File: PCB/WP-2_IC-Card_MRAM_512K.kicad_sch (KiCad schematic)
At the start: 25 parts, among them J1 SMS-138-01-G-S, SW1 CUS-14TB, U1 MR2A08xxYSxxx, U2 MIC5317-3.3YD5, U3 4245, U4 4245, U5 4245, U6 4245

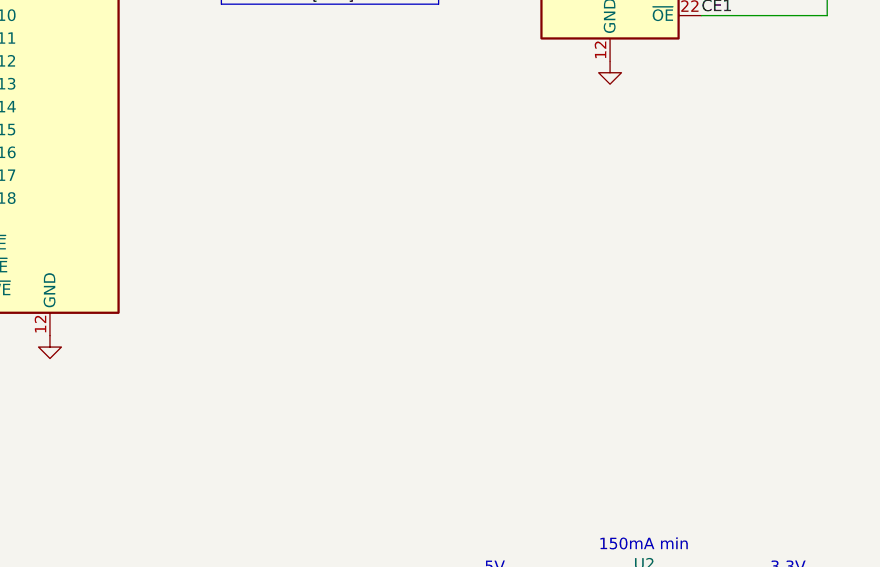
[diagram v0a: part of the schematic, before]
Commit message: mram specify industrial part
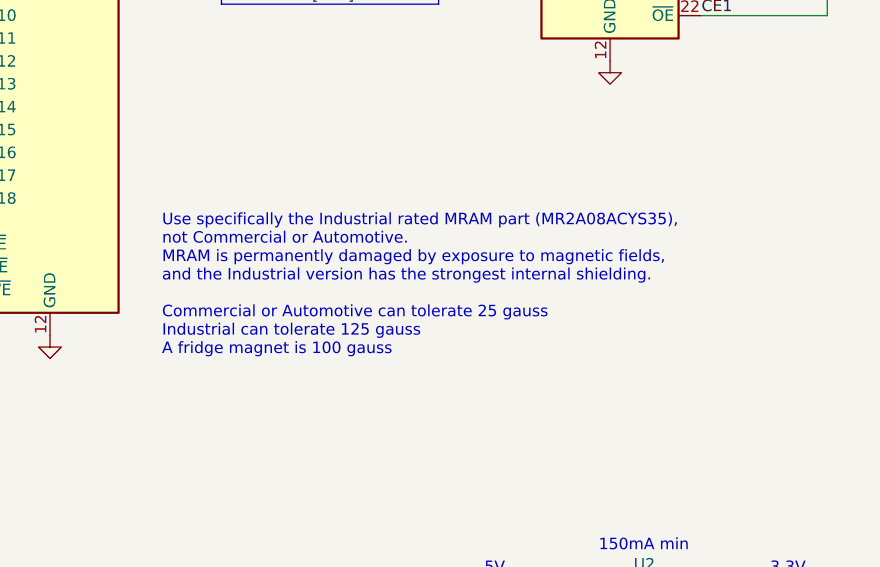
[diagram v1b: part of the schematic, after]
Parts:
- U1: MPN MR2A08AYS35 -> MR2A08ACYS35
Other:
- note added: "Use specifically the Industrial rated MRAM part (MR2A08ACYS35), not Commercial or Automotive. MRAM is permanently damaged by exposure to magnetic fields, and the Industrial version has the strongest internal shielding. Commercial or Automotive can tolerate 25 gauss Industrial can tolerate 125 gauss A fridge magnet is 100 gauss"
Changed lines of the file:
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@@
 		)
 	)
+	(text "Use specifically the Industrial rated MRAM part (MR2A08ACYS35),\nnot Commercial or Automotive.\nMRAM is permanently damaged by exposure to magnetic fields,\nand the Industrial version has the strongest internal shielding.\n\nCommercial or Automotive can tolerate 25 gauss\nIndustrial can tolerate 125 gauss\nA fridge magnet is 100 gauss\n"
+		(exclude_from_sim no)
+		(at 177.546 102.108 0)
+		(effects
+			(font
+				(size 1.27 1.27)
+			)
+			(justify left top)
+		)
+	)
 	(text "5V"
 		(exclude_from_sim no)
@@
 			)
 		)
-		(property "MPN" "MR2A08AYS35"
+		(property "MPN" "MR2A08ACYS35"
 			(at 165.1 82.55 0)
 			(effects

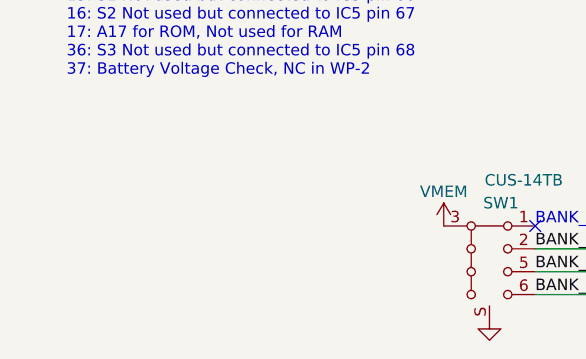
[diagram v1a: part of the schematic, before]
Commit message: local symbol & footprint library organization, add shielded mram version
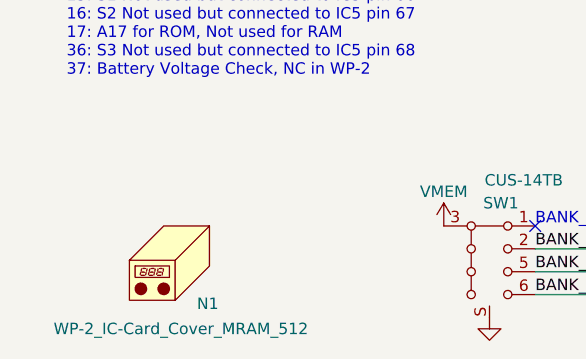
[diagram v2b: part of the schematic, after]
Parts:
- added N1: WP-2_IC-Card_Cover_MRAM_512, 000_LOCAL:WP-2_IC_Card_Cover_MRAM_512, symbol 000_LOCAL:Housing
- C1, C10, C11, C12, C2, C3, C4, C5, C6, C7, C8, C9: footprint 0_LOCAL:C_0805_1mm -> 000_LOCAL:C_0805_1mm; symbol 0_LOCAL:C_Small -> 000_LOCAL:C_Small
- D1: footprint 0_LOCAL:TSSOP-6-symmetric -> 000_LOCAL:TSSOP-6-symmetric; symbol 0_LOCAL:BAT54CDW -> 000_LOCAL:BAT54CDW
- J1: footprint 0_LOCAL:SMS-138-01-x-x_edge -> 000_LOCAL:SMS-138-01-x-x_pcb_edge; symbol 0_LOCAL:Conn_01x38_Female -> 000_LOCAL:Conn_01x38_Female
- R1, R2, R3, R4: footprint 0_LOCAL:R_0805 -> 000_LOCAL:R_0805; symbol 0_LOCAL:R -> 000_LOCAL:R
- SW1: footprint 0_LOCAL:SW_SP4T_CUS-14B pth -> 000_LOCAL:SW_SP4T_CUS-14B pth; symbol 0_LOCAL:SW_1P4T_CUS-14B -> 000_LOCAL:SW_1P4T_CUS-14B
- U1: footprint 0_LOCAL:TSOP-II-44_10.16x18.41mm_P0.8mm -> 000_LOCAL:TSOP-II-44_10.16x18.41mm_P0.8mm; symbol 0_LOCAL:MR2A08xxYSxxx -> 000_LOCAL:MR2A08xxYSxxx
- U2: footprint 0_LOCAL:TSOT-23-5 -> 000_LOCAL:TSOT-23-5; symbol 0_LOCAL:MIC5365-3.3YD5 -> 000_LOCAL:MIC5365-3.3YD5
- U3, U4, U5, U6: footprint 0_LOCAL:TSSOP-24_4.4x7.8mm_P0.65mm -> 000_LOCAL:TSSOP-24_4.4x7.8mm_P0.65mm; symbol 0_LOCAL:4245 -> 000_LOCAL:4245

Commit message: cleanup names, cover inside corner reliefs
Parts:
- N1: footprint 000_LOCAL:WP-2_IC_Card_Cover_MRAM_512 -> 000_LOCAL:WP-2_IC-Card_Cover_MRAM_512; now left out of the parts list
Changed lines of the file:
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@@
 		(unit 1)
 		(exclude_from_sim yes)
-		(in_bom yes)
+		(in_bom no)
 		(on_board yes)
 		(dnp no)
@@
 			)
 		)
-		(property "Footprint" "000_LOCAL:WP-2_IC_Card_Cover_MRAM_512"
+		(property "Footprint" "000_LOCAL:WP-2_IC-Card_Cover_MRAM_512"
 			(at 33.02 182.88 0)
 			(effects

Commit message: rom wren sw, boms, footprints, shielded mram
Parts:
- C1, C10, C11, C12, C2, C3, C4, C5, C6, C7, C8, C9: footprint 000_LOCAL:C_0805_1mm -> 000_LOCAL:C_0805; MPN CL21B105KBFNFNE -> CL21A105KBCLNNC

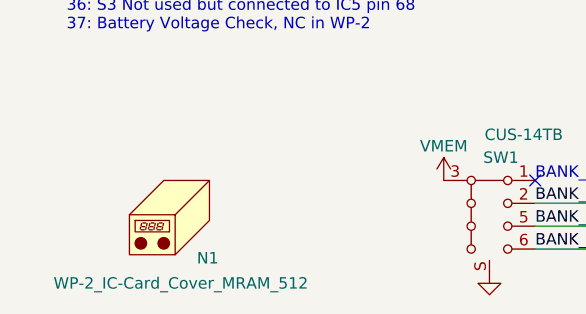
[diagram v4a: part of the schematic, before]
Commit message: update covers for flash & mram with bank sw & write sw
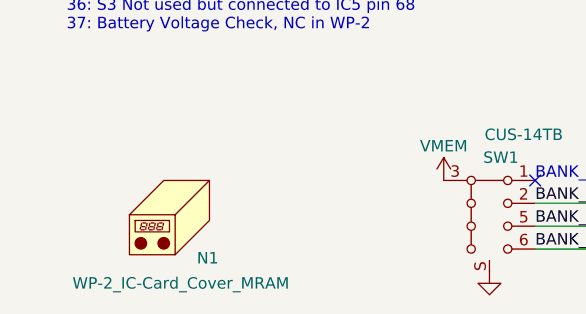
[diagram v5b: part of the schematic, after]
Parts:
- N1: value WP-2_IC-Card_Cover_MRAM_512 -> WP-2_IC-Card_Cover_MRAM; footprint 000_LOCAL:WP-2_IC-Card_Cover_MRAM_512 -> 000_LOCAL:WP-2_IC-Card_Cover_MRAM
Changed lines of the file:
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@@
 			)
 		)
-		(property "Value" "WP-2_IC-Card_Cover_MRAM_512"
+		(property "Value" "WP-2_IC-Card_Cover_MRAM"
 			(at 31.75 191.77 0)
 			(effects
@@
 			)
 		)
-		(property "Footprint" "000_LOCAL:WP-2_IC-Card_Cover_MRAM_512"
+		(property "Footprint" "000_LOCAL:WP-2_IC-Card_Cover_MRAM"
 			(at 33.02 182.88 0)
 			(effects
